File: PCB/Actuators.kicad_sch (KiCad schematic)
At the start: 0 parts

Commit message: [Schem] Uhh made the Amplifier & motor driver circuits
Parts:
- added C1, C22: 1uF, symbol Device:C
- added C13, C14, C17, C18: 220 pF, symbol Device:C
- added C15, C20: 0.1 uF, symbol Device:C
- added C16, C19: 10uF, symbol Device:C
- added C21, C23: 100 pF, symbol Device:C
- added FB3, FB4, FB5, FB6: F, symbol Device:FerriteBead_Small
- added J1, J6: R_Motor, symbol Connector:Screw_Terminal_01x02
- added J3: Left_Speaker, symbol Connector:Screw_Terminal_01x02
- added J4: Right_Speaker, symbol Connector:Screw_Terminal_01x02
- added J5: GAIN_sel, symbol Connector_Generic:Conn_01x03
- added R10, R2: 50K, symbol Device:R
- added R11: 370K, symbol Device:R
- added R12, R13, R14, R15, R16, R17, R18, R19, R20, R21, R22, R23, R28, R29, R30, R31: 10k, symbol Device:R
- added U10, U5, U6, U9: BTN7960B, BTN7960B:IC_BTN7960B, symbol WALL-E_symbols:BTN7960B
- added U2, U4: MAX98357A, Package_DFN_QFN:TQFN-16-1EP_3x3mm_P0.5mm_EP1.23x1.23mm, symbol Audio:MAX98357A
- added U7, U8: 74HC244, symbol 74xx:74HC244
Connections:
- new net: U10.3 (INH), U8.12 (1Y3)
- new net: U10.2 (IN), U8.14 (1Y2)
- new net: U8.16 (1Y1), U9.3 (INH)
- new net: U8.18 (1Y0), U9.2 (IN)
- new net: C14.2, FB3.1, J3.2 (Pin_2)
- new net: FB3.2, U4.10 (OUTN)
- new net: J5.1 (Pin_1), R10.2
- new net: R31.2, U10.5 (SR)
- new net: R12.1, U6.5 (SR)
- new net: U5.3 (INH), U7.12 (1Y3)
- new net: U5.2 (IN), U7.14 (1Y2)
- new net: U6.3 (INH), U7.16 (1Y1)
- new net: U6.2 (IN), U7.18 (1Y0)
- new net: J5.3 (Pin_3), R2.1
- new net: C17.2, FB6.1, J4.2 (Pin_2)
- new net: FB6.2, U2.10 (OUTN)
- new net: C18.2, FB5.2, J4.1 (Pin_1)
- new net: R14.1, U9.5 (SR)
- new net: C13.2, FB4.2, J3.1 (Pin_1)
- new net: FB4.1, U4.9 (OUTP)
- new net: R29.2, U5.5 (SR)
- new net: FB5.1, U2.9 (OUTP)
- new net: R11.1, U2.4 (~{SD_MODE})
- new net +12V: C21.1, C23.1, U10.7 (VS), U5.7 (VS), U6.7 (VS), U9.7 (VS)
- new net +5V: C1.1, C22.1, U7.20 (VCC), U8.20 (VCC)
- new net BCLK: U2.16 (BCLK), U4.16 (BCLK)
- new net DIN: U2.1 (DIN), U4.1 (DIN)
- new net GAIN: J5.2 (Pin_2), U2.2 (GAIN_SLOT), U4.2 (GAIN_SLOT)
- new net GND: C1.2, C13.1, C14.1, C15.1, C16.1, C17.1, C18.1, C19.1, C20.1, C21.2, C22.2, C23.2, R12.2, R13.2, R14.2, R15.2, R16.2, R17.2, R18.2, R19.2, R2.2, R20.2, R21.2, R22.2, R23.2, R28.2, R29.1, R30.2, R31.1, U10.1 (GND), U2.11 (GND), U2.15 (GND), U2.17 (PAD), U2.3 (GND), U4.11 (GND), U4.15 (GND), U4.17 (PAD), U4.3 (GND), U5.1 (GND), U6.1 (GND), U7.1 (1OE), U7.10 (GND), U7.11 (2A3), U7.13 (2A2), U7.15 (2A1), U7.17 (2A0), U7.19 (2OE), U8.1 (1OE), U8.10 (GND), U8.11 (2A3), U8.13 (2A2), U8.15 (2A1), U8.17 (2A0), U8.19 (2OE), U9.1 (GND)
- new net LM+: J6.1 (Pin_1), U9.4 (OUT), U9.8 (OUT)
- new net LM-: J6.2 (Pin_2), U10.4 (OUT), U10.8 (OUT)
- new net LRCLK: U2.14 (LRCLK), U4.14 (LRCLK)
- new net L_EN (LM): R23.1, U8.8 (1A3)
- new net L_EN (RM): R19.1, U7.8 (1A3)
- new net L_IS (LM): R30.1, U10.6 (IS)
- new net L_IS (RM): R28.1, U5.6 (IS)
- new net L_PWM (LM): R22.1, U8.6 (1A2)
- new net L_PWM (RM): R18.1, U7.6 (1A2)
- new net RM+: J1.1 (Pin_1), U6.4 (OUT), U6.8 (OUT)
- new net RM-: J1.2 (Pin_2), U5.4 (OUT), U5.8 (OUT)
- new net R_EN (LM): R21.1, U8.4 (1A1)
- new net R_EN (RM): R17.1, U7.4 (1A1)
- new net R_IS (LM): R15.1, U9.6 (IS)
- new net R_IS (RM): R13.1, U6.6 (IS)
- new net R_PWM (LM): R20.1, U8.2 (1A0)
- new net R_PWM (RM): R16.1, U7.2 (1A0)
- new net VCC: C15.2, C16.2, C19.2, C20.2, R10.1, R11.2, U2.7 (VDD), U2.8 (VDD), U4.4 (~{SD_MODE}), U4.7 (VDD), U4.8 (VDD)
- no-connect marks 0 -> 8

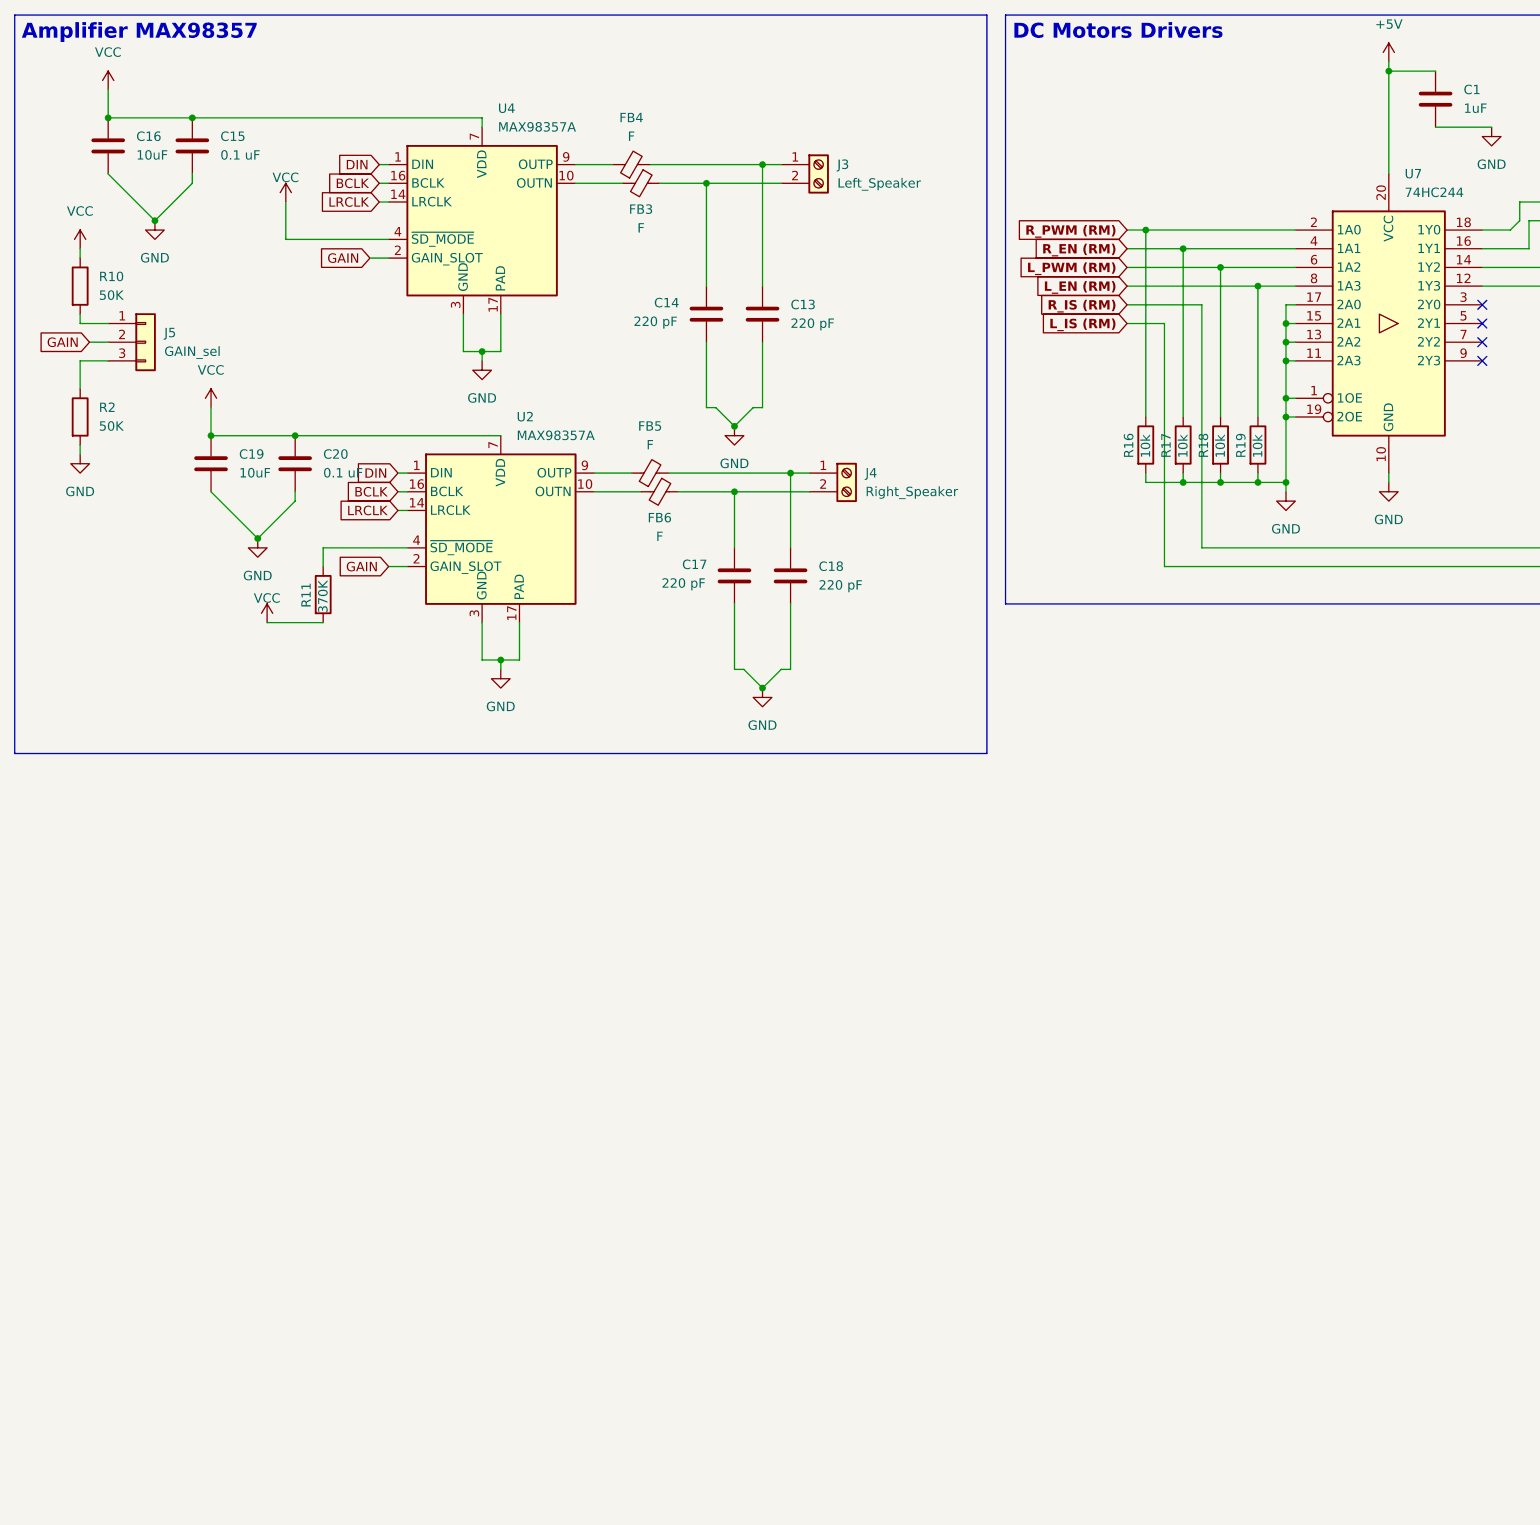
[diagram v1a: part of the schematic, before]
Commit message: [Schem] Made the servo controller
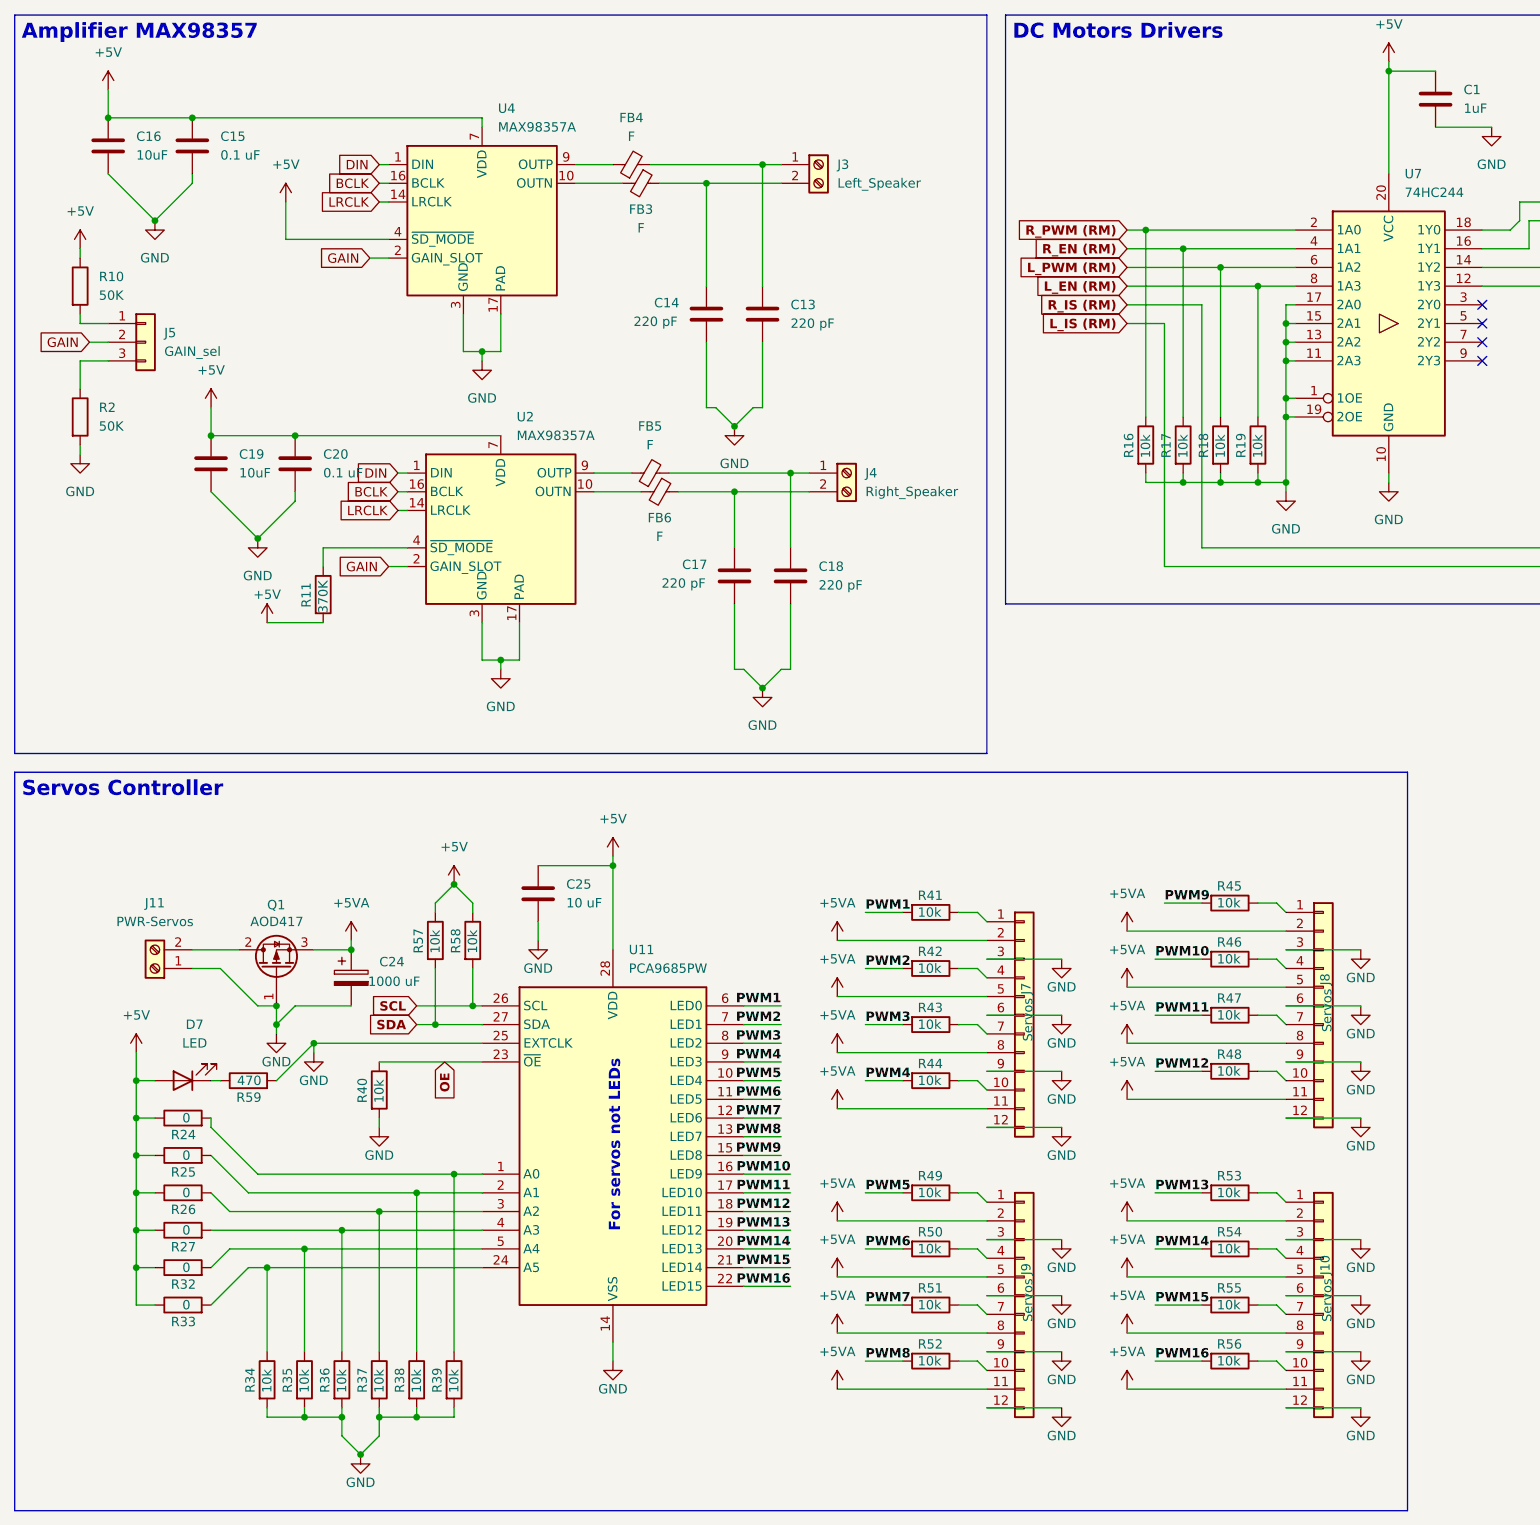
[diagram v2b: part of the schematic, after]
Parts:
- added C24: 1000 uF, symbol Device:C_Polarized
- added C25: 10 uF, symbol Device:C
- added D7: LED, symbol Device:LED
- added J10, J7, J8, J9: Servos, symbol Connector_Generic:Conn_01x12
- added J11: PWR-Servos, symbol Connector:Screw_Terminal_01x02
- added Q1: AOD417, symbol Transistor_FET:Q_PMOS_GDS
- added R24, R25, R26, R27, R32, R33: 0, symbol Device:R
- added R34, R35, R36, R37, R38, R39, R40, R41, R42, R43, R44, R45, R46, R47, R48, R49, R50, R51, R52, R53, R54, R55, R56, R57, R58: 10k, symbol Device:R
- added R59: 470, symbol Device:R
- added U11: PCA9685PW, Package_SO:TSSOP-28_4.4x9.7mm_P0.65mm, symbol Driver_LED:PCA9685PW
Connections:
- net VCC is gone; now on net +5V: C15.2, C16.2, C19.2, C20.2, R10.1, R11.2, U2.7 (VDD), U2.8 (VDD), U4.4 (~{SD_MODE}), U4.7 (VDD), U4.8 (VDD)
- net +5V: now also C25.1, D7.2 (A), R24.1, R25.1, R26.1, R27.1, R32.1, R33.1, R57.1, R58.1, U11.28 (VDD)
- net GND: now also C24.2, C25.2, J10.12 (Pin_12), J10.3 (Pin_3), J10.6 (Pin_6), J10.9 (Pin_9), J11.1 (Pin_1), J7.12 (Pin_12), J7.3 (Pin_3), J7.6 (Pin_6), J7.9 (Pin_9), J8.12 (Pin_12), J8.3 (Pin_3), J8.6 (Pin_6), J8.9 (Pin_9), J9.12 (Pin_12), J9.3 (Pin_3), J9.6 (Pin_6), J9.9 (Pin_9), Q1.1 (G), R34.2, R35.2, R36.2, R37.2, R38.2, R39.2, R40.2, R59.2, U11.14 (VSS), U11.25 (EXTCLK)
- new net: J9.1 (Pin_1), R49.1
- new net: J9.10 (Pin_10), R52.1
- new net: J9.4 (Pin_4), R50.1
- new net: J9.7 (Pin_7), R51.1
- new net: J7.1 (Pin_1), R41.1
- new net: R33.2, R34.1, U11.24 (A5)
- new net: J7.4 (Pin_4), R42.1
- new net: J11.2 (Pin_2), Q1.2 (D)
- new net: J10.10 (Pin_10), R56.1
- new net: R27.2, R36.1, U11.4 (A3)
- new net: R24.2, R39.1, U11.1 (A0)
- new net: R25.2, R38.1, U11.2 (A1)
- new net: R26.2, R37.1, U11.3 (A2)
- new net: R32.2, R35.1, U11.5 (A4)
- new net: J8.1 (Pin_1), R45.1
- new net: J8.10 (Pin_10), R48.1
- new net: J8.4 (Pin_4), R46.1
- new net: J8.7 (Pin_7), R47.1
- new net: J10.4 (Pin_4), R54.1
- new net: J10.7 (Pin_7), R55.1
- new net: D7.1 (K), R59.1
- new net: J7.7 (Pin_7), R43.1
- new net: J7.10 (Pin_10), R44.1
- new net: J10.1 (Pin_1), R53.1
- new net +5VA: C24.1, J10.11 (Pin_11), J10.2 (Pin_2), J10.5 (Pin_5), J10.8 (Pin_8), J7.11 (Pin_11), J7.2 (Pin_2), J7.5 (Pin_5), J7.8 (Pin_8), J8.11 (Pin_11), J8.2 (Pin_2), J8.5 (Pin_5), J8.8 (Pin_8), J9.11 (Pin_11), J9.2 (Pin_2), J9.5 (Pin_5), J9.8 (Pin_8), Q1.3 (S)
- new net OE: R40.1, U11.23 (~{OE})
- new net PWM1: R41.2, U11.6 (LED0)
- new net PWM10: R46.2, U11.16 (LED9)
- new net PWM11: R47.2, U11.17 (LED10)
- new net PWM12: R48.2, U11.18 (LED11)
- new net PWM13: R53.2, U11.19 (LED12)
- new net PWM14: R54.2, U11.20 (LED13)
- new net PWM15: R55.2, U11.21 (LED14)
- new net PWM16: R56.2, U11.22 (LED15)
- new net PWM2: R42.2, U11.7 (LED1)
- new net PWM3: R43.2, U11.8 (LED2)
- new net PWM4: R44.2, U11.9 (LED3)
- new net PWM5: R49.2, U11.10 (LED4)
- new net PWM6: R50.2, U11.11 (LED5)
- new net PWM7: R51.2, U11.12 (LED6)
- new net PWM8: R52.2, U11.13 (LED7)
- new net PWM9: R45.2, U11.15 (LED8)
- new net SCL: R58.2, U11.26 (SCL)
- new net SDA: R57.2, U11.27 (SDA)
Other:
- note added: "For servos not LEDs"

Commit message: [Schem] Finished the Hierarchy Labels of all the pages
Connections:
- net L_EN (LM) renamed L_EN_(LM)
- net L_EN (RM) renamed L_EN_(RM)
- net L_IS (LM) renamed L_IS_(LM)
- net L_IS (RM) renamed L_IS_(RM)
- net L_PWM (LM) renamed L_PWM_(LM)
- net L_PWM (RM) renamed L_PWM_(RM)
- net R_EN (LM) renamed R_EN_(LM)
- net R_EN (RM) renamed R_EN_(RM)
- net R_IS (LM) renamed R_IS_(LM)
- net R_IS (RM) renamed R_IS_(RM)
- net R_PWM (LM) renamed R_PWM_(LM)
- net R_PWM (RM) renamed R_PWM_(RM)

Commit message: [Schem] Added all the net labels and connected the Dashboard screen
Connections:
- net SCL renamed Ser_SCL
- net SDA renamed Ser_SDA
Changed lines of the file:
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@@
 		)
 	)
-	(hierarchical_label "SCL"
+	(hierarchical_label "Ser_SCL"
 		(shape input)
 		(at 68.58 149.86 180)
@@
 		)
 	)
-	(hierarchical_label "SDA"
+	(hierarchical_label "Ser_SDA"
 		(shape input)
 		(at 68.58 152.4 180)

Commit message: [PCB] Assigned all the footprints
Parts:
- C1, C13, C14, C15, C16, C17, C18, C19, C20, C21, C22, C23, C25, FB3, FB4, FB5, FB6: footprint (none) -> Capacitor_SMD:C_0603_1608Metric_Pad1.08x0.95mm_HandSolder
- C24: footprint (none) -> Capacitor_THT:CP_Radial_D8.0mm_P2.50mm
- D7: footprint (none) -> LED_SMD:LED_0603_1608Metric_Pad1.05x0.95mm_HandSolder
- J1, J11: footprint (none) -> TerminalBlock_Altech:Altech_AK100_1x02_P5.00mm
- J10, J7, J8, J9: footprint (none) -> Wall_E_FPs:Free_GPIO_FP
- J3, J4: footprint (none) -> Connector_JST:JST_ZH_B2B-ZR-SM4-TF_1x02-1MP_P1.50mm_Vertical
- J5: footprint (none) -> Jumper:SolderJumper-3_P1.3mm_Open_Pad1.0x1.5mm
- J6: value R_Motor -> L_Motor; footprint (none) -> TerminalBlock_Altech:Altech_AK100_1x02_P5.00mm
- Q1: footprint (none) -> Package_TO_SOT_SMD:TO-252-3_TabPin2
- R10, R11, R12, R13, R14, R15, R16, R17, R18, R19, R2, R20, R21, R22, R23, R24, R25, R26, R27, R28, R29, R30, R31, R32, R33, R34, R35, R36, R37, R38, R39, R40, R41, R42, R43, R44, R45, R46, R47, R48, R49, R50, R51, R52, R53, R54, R55, R56, R57, R58, R59: footprint (none) -> Resistor_SMD:R_0603_1608Metric_Pad0.98x0.95mm_HandSolder
- U10, U5, U6, U9: footprint BTN7960B:IC_BTN7960B -> Wall_E_FPs:IC_BTN7960B
- U11: footprint Package_SO:TSSOP-28_4.4x9.7mm_P0.65mm -> Package_SO:TSSOP-28-1EP_4.4x9.7mm_P0.65mm_EP2.74x4.75mm_ThermalVias
- U7, U8: footprint (none) -> Package_SO:TSSOP-28_4.4x9.7mm_P0.65mm
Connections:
- net OE: no longer names the net of R40.1, U11.23 (~{OE})

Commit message: [PCB] Traced the ESP's Type C
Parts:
- U11: footprint Package_SO:TSSOP-28-1EP_4.4x9.7mm_P0.65mm_EP2.74x4.75mm_ThermalVias -> Package_SO:TSSOP-28_4.4x9.7mm_P0.65mm
- U7, U8: footprint Package_SO:TSSOP-28_4.4x9.7mm_P0.65mm -> Package_SO:TSSOP-20_4.4x6.5mm_P0.65mm
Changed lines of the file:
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@@
 			)
 		)
-		(property "Footprint" "Package_SO:TSSOP-28_4.4x9.7mm_P0.65mm"
+		(property "Footprint" "Package_SO:TSSOP-20_4.4x6.5mm_P0.65mm"
 			(at 370.84 58.42 0)
 			(hide yes)
@@
 			)
 		)
-		(property "Footprint" "Package_SO:TSSOP-28_4.4x9.7mm_P0.65mm"
+		(property "Footprint" "Package_SO:TSSOP-20_4.4x6.5mm_P0.65mm"
 			(at 200.66 57.15 0)
 			(hide yes)
@@
 			)
 		)
-		(property "Footprint" "Package_SO:TSSOP-28-1EP_4.4x9.7mm_P0.65mm_EP2.74x4.75mm_ThermalVias"
+		(property "Footprint" "Package_SO:TSSOP-28_4.4x9.7mm_P0.65mm"
 			(at 95.885 192.405 0)
 			(hide yes)
